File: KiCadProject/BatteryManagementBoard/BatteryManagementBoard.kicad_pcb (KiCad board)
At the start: 6 copper layers, 45 x 45 mm, 86 parts, among them J201 USB-C-2.0, J202 XT30, J203 Conn_02x05, J204 XT60, J205 Conn_02x05, J206 Conn_01x02_Male, J207 Conn_01x05_Male, J208 JST_B5B_XH, Q301 NFET_Gatenames, Q302 NFET_Gatenames, Q303 NFET_Gatenames, Q304 NFET_Gatenames, Q305 PMOS_Gatenames, U301 BQ25713, U401 BD433M5FP, U501 PTN5150

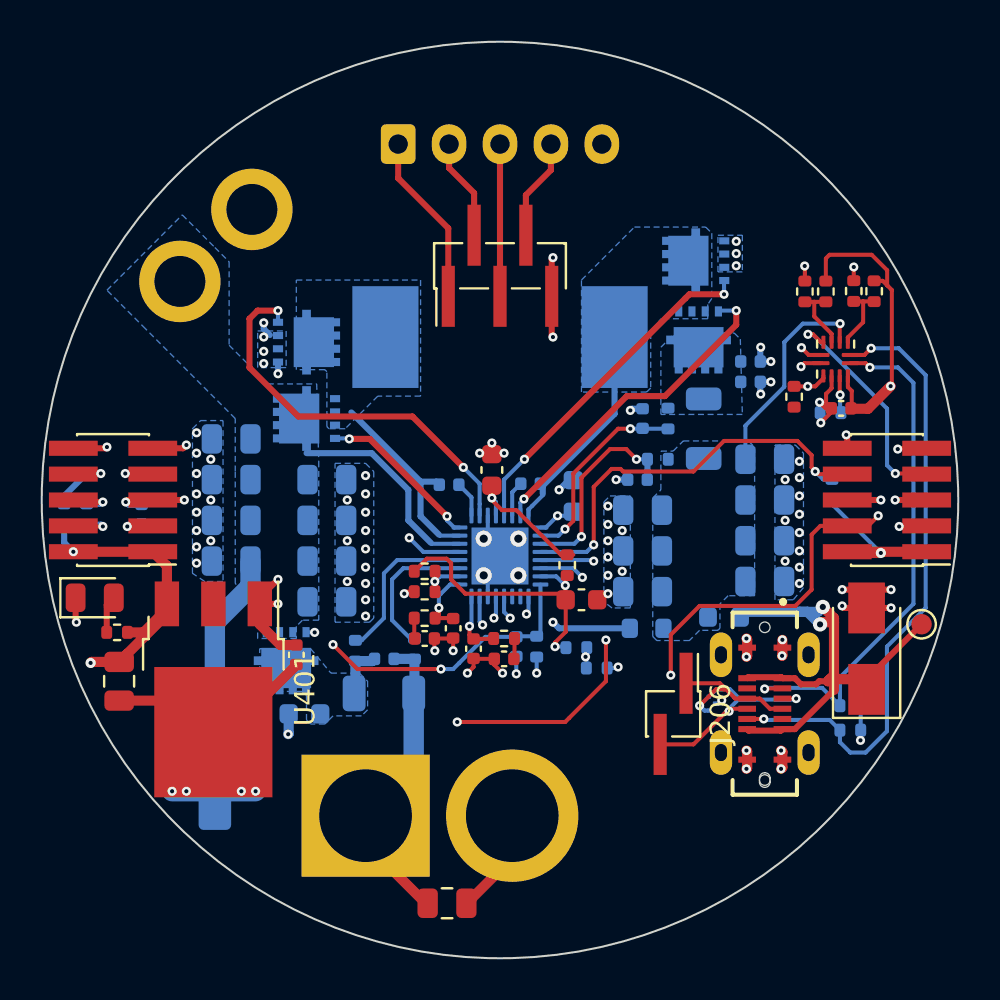
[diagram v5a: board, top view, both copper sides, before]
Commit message: Finished v0.1 of BatMan PCB, started layout of ESP PCB
Signed-off-by: Eldalote.Electronics <Eldalote.Electronics@gmail.com>
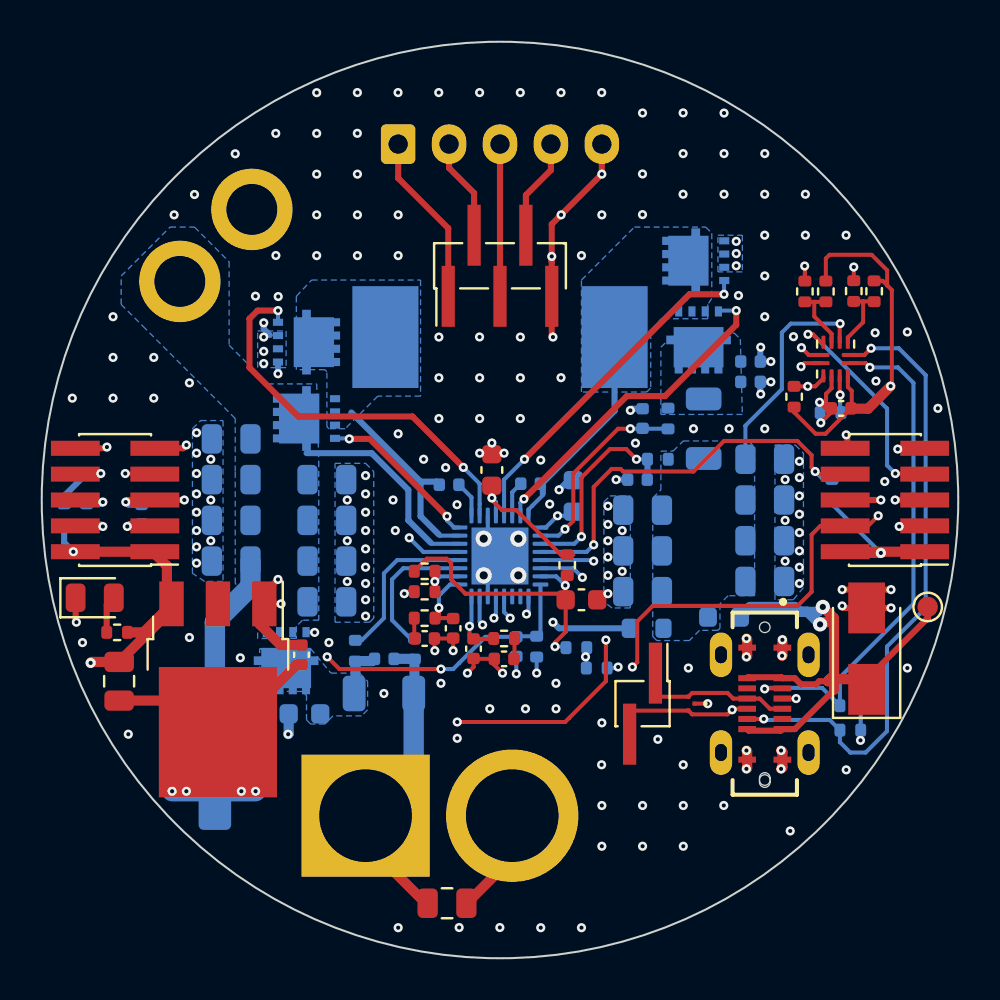
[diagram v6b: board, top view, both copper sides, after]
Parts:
- D202: moved to F.Cu
- moved J206 1.58 mm to (157.0, 110.0)
- moved D202 1.00 mm to (159.4, 110.0)
- moved TP201 0.90 mm to (171.0, 105.2)
- moved C402 0.25 mm to (140.2, 107.6)
- moved U401 0.22 mm to (136.2, 109.3)
- moved J203 0.10 mm to (168.9, 100.0)
- moved J205 0.10 mm to (131.1, 100.0)
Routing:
- net GND: track 76.9 -> 83.7 mm, vias 106 -> 221
- net +3.3V: track 110.0 -> 113.4 mm
- net /P2-Connectors/VBUS_connector: track 26.9 -> 28.0 mm
- net BQ_IADPT: track 31.7 -> 31.2 mm
- net /P2-Connectors/USB-N: track 7.40 -> 7.76 mm, vias 1 -> 0
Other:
- board text added: "Battery"
- board text added: "LED power"

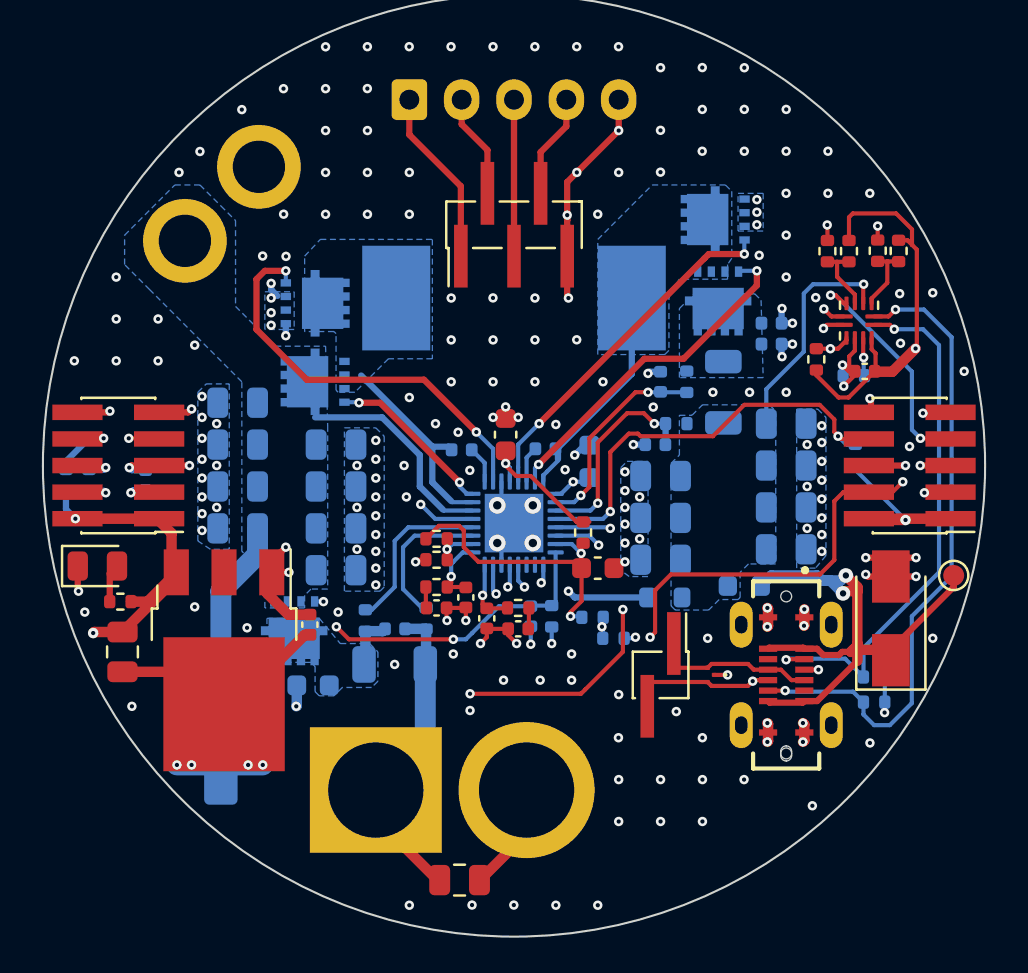
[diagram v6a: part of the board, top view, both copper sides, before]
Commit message: All PCB's should be done. Do a final check before ordering.
Signed-off-by: Eldalote.Electronics <Eldalote.Electronics@gmail.com>
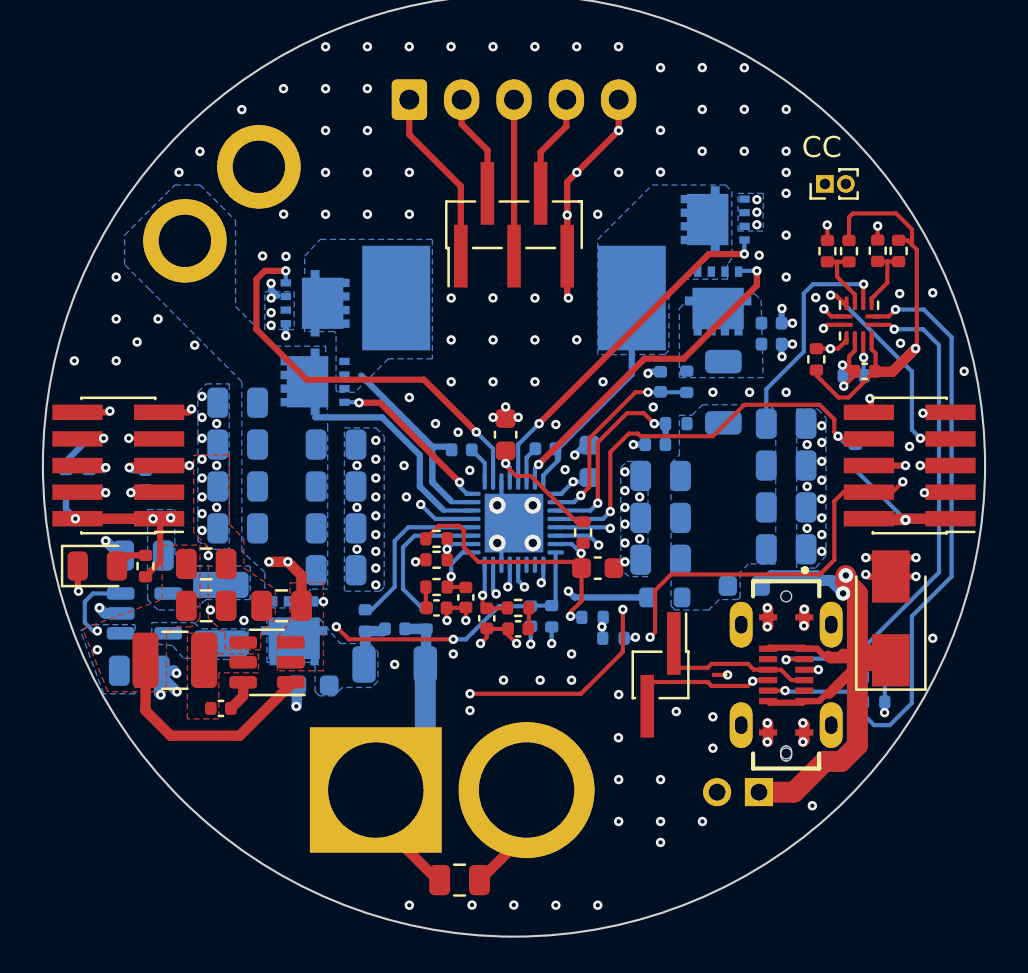
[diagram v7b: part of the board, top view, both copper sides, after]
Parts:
- removed C401: 22u, Capacitor_SMD:CP_Elec_5x5.3
- removed TP201: TestPoint, TestPoint:TestPoint_Pad_D1.0mm
- added C404: 22u, Capacitor_SMD:C_0805_2012Metric, F.Cu at (135.3, 106.7)
- added C405: 22u, Capacitor_SMD:C_0805_2012Metric, F.Cu at (135.3, 104.7)
- added C406: 10u, Capacitor_SMD:C_0805_2012Metric, B.Cu at (132.1, 109.8)
- added C407: 22u, Capacitor_SMD:C_0805_2012Metric, B.Cu at (132.3, 104.3)
- added J209: Optional off board USB power connection, Connector_PinHeader_2.00mm:PinHeader_1x02_P2.00mm_Vertical, B.Cu at (161.7, 115.6)
- added J210: Optional off board USB CC connection, Connector_PinHeader_1.00mm:PinHeader_1x02_P1.00mm_Vertical, F.Cu at (164.8, 86.5)
- added L401: 4u7, Inductor_SMD:L_1210_3225Metric, F.Cu at (133.8, 109.3)
- added L402: 1u, Inductor_SMD:L_1210_3225Metric, B.Cu at (136.0, 107.1)
- added U402: SC189, Package_TO_SOT_SMD:SOT-23-5, B.Cu at (132.3, 107.1)
- C402: value 100n -> 10u; footprint Capacitor_SMD:C_0402_1005Metric -> Capacitor_SMD:C_0805_2012Metric
- C403: value 10u -> 100n; footprint Capacitor_SMD:C_0805_2012Metric -> Capacitor_SMD:C_0402_1005Metric
- U401: value BD433M5FP -> AP63205WU; footprint Package_TO_SOT_SMD:TO-252-3_TabPin4 -> Package_TO_SOT_SMD:TSOT-23-6
- moved C403 5.42 mm to (136.0, 111.6), turned to 0 degrees
- moved R401 2.08 mm to (132.4, 104.8), turned to 90 degrees
- moved U401 2.05 mm to (138.2, 109.4), turned to 180 degrees
- moved C402 1.62 mm to (138.9, 106.7), turned to 180 degrees
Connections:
- C403 pad 1: +3.3V -> /P4 - 3V3 Regulator/APSW
- C403 pad 2: GND -> /P4 - 3V3 Regulator/APBST
- U401 pad 1: VOUT -> +5V
- U401 pad 2: unconnected-(U401-Pad2) -> VOUT
- U401 pad 3: +3.3V -> VOUT
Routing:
- net +5V: track 0.00 -> 14.6 mm, vias 0 -> 2
- net /P2-Connectors/VBUS_connector: track 28.0 -> 40.8 mm
- net VOUT: track 24.1 -> 13.5 mm
- net GND: track 83.7 -> 74.5 mm, vias 221 -> 216
- net CC1: track 25.8 -> 35.0 mm
- net CC2: track 31.0 -> 38.4 mm
- net +3.3V: track 113.4 -> 111.2 mm, vias 4 -> 5
- net /P4 - 3V3 Regulator/APBST: track 0.00 -> 1.49 mm
- added copper zone on B.Cu, net +3.3V
- added copper zone on B.Cu, net +5V
- added copper zone on F.Cu, net +5V
- added copper zone on F.Cu, net /P4 - 3V3 Regulator/APSW
- added copper zone on B.Cu, net /P4 - 3V3 Regulator/scLX
- added copper zone on F.Cu, net GND
- added copper zone on F.Cu, net VOUT
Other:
- board text added: "BM V0.3"
- board text added: "CC"
- board text added: "JM Liewes"
- board text added: "jlcjlcjlcjlc"

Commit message: Made ready to order PCBs. Some problems with ordering due to misunderstanding. Thinking about solutions
Signed-off-by: Eldalote.Electronics <Eldalote.Electronics@gmail.com>
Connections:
- net /P5-TUSB422 (Optional)/PTN_ADR renamed /P5-PTN5150 (Optional)/PTN_ADR
- net /P5-TUSB422 (Optional)/PTN_ENB renamed /P5-PTN5150 (Optional)/PTN_ENB
- net /P5-TUSB422 (Optional)/PTN_PORT renamed /P5-PTN5150 (Optional)/PTN_PORT
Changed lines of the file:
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@@
       (layerselection 0x00010fc_ffffffff)
       (disableapertmacros false)
-      (usegerberextensions false)
+      (usegerberextensions true)
       (usegerberattributes true)
-      (usegerberadvancedattributes true)
-      (creategerberjobfile true)
+      (usegerberadvancedattributes false)
+      (creategerberjobfile false)
       (svguseinch false)
       (svgprecision 6)
@@
       (plotinvisibletext false)
       (sketchpadsonfab false)
-      (subtractmaskfromsilk false)
+      (subtractmaskfromsilk true)
       (outputformat 1)
       (mirror false)
@@
   (net 55 "/P2-Connectors/Cell2")
   (net 56 "/P2-Connectors/Cell1")
-  (net 57 "/P5-TUSB422 (Optional)/PTN_ADR")
-  (net 58 "/P5-TUSB422 (Optional)/PTN_PORT")
-  (net 59 "/P5-TUSB422 (Optional)/PTN_ENB")
+  (net 57 "/P5-PTN5150 (Optional)/PTN_ADR")
+  (net 58 "/P5-PTN5150 (Optional)/PTN_PORT")
+  (net 59 "/P5-PTN5150 (Optional)/PTN_ENB")
   (net 60 "PTN_ID")
   (net 61 "/P4 - 3V3 Regulator/APBST")
@@
     (descr "Texas  X2QFN, 12 Pin (http://www.ti.com/lit/ml/mpqf391c/mpqf391c.pdf), generated with kicad-footprint-generator ipc_noLead_generator.py")
     (tags "Texas X2QFN NoLead")
-    (property "Sheetfile" "P5TUSB422.kicad_sch")
-    (property "Sheetname" "P5-TUSB422 (Optional)")
+    (property "Sheetfile" "P5PTN5150.kicad_sch")
+    (property "Sheetname" "P5-PTN5150 (Optional)")
     (clearance 0.13)
     (attr smd)
@@
       (net 28 "CC2") (pinfunction "CC2") (pintype "passive"))
     (pad "3" smd roundrect (at -0.6 0.825 180) (size 0.2 0.65) (layers "F.Cu" "F.Paste" "F.Mask") (roundrect_rratio 0.25)
-      (net 58 "/P5-TUSB422 (Optional)/PTN_PORT") (pinfunction "PORT") (pintype "passive"))
+      (net 58 "/P5-PTN5150 (Optional)/PTN_PORT") (pinfunction "PORT") (pintype "passive"))
     (pad "4" smd roundrect (at -0.2 0.825 180) (size 0.2 0.65) (layers "F.Cu" "F.Paste" "F.Mask") (roundrect_rratio 0.25)
       (net 1 "VBUS") (pinfunction "VBUS_DET") (pintype "passive"))
     (pad "5" smd roundrect (at 0.2 0.825 180) (size 0.2 0.65) (layers "F.Cu" "F.Paste" "F.Mask") (roundrect_rratio 0.25)
-      (net 57 "/P5-TUSB422 (Optional)/PTN_ADR") (pinfunction "ADR/CON_DET") (pintype "passive"))
+      (net 57 "/P5-PTN5150 (Optional)/PTN_ADR") (pinfunction "ADR/CON_DET") (pintype "passive"))
     (pad "6" smd roundrect (at 0.6 0.825 180) (size 0.2 0.65) (layers "F.Cu" "F.Paste" "F.Mask") (roundrect_rratio 0.25)
       (net 34 "USBC_INT") (pinfunction "INTB") (pintype "passive"))
@@
       (net 2 "GND") (pinfunction "GND") (pintype "passive"))
     (pad "11" smd roundrect (at -0.2 -0.825 180) (size 0.2 0.65) (layers "F.Cu" "F.Paste" "F.Mask") (roundrect_rratio 0.25)
-      (net 59 "/P5-TUSB422 (Optional)/PTN_ENB") (pinfunction "ENB") (pintype "passive"))
+      (net 59 "/P5-PTN5150 (Optional)/PTN_ENB") (pinfunction "ENB") (pintype "passive"))
     (pad "12" smd roundrect (at -0.6 -0.825 180) (size 0.2 0.65) (layers "F.Cu" "F.Paste" "F.Mask") (roundrect_rratio 0.25)
       (net 22 "+3.3V") (pinfunction "VDD") (pintype "passive"))
@@
     (property "Extra Requirement" "25V")
     (property "MfID" "CL05A104KA5NNNC")
-    (property "Sheetfile" "P5TUSB422.kicad_sch")
-    (property "Sheetname" "P5-TUSB422 (Optional)")
+    (property "Sheetfile" "P5PTN5150.kicad_sch")
+    (property "Sheetname" "P5-PTN5150 (Optional)")
     (attr smd)
     (fp_text reference "C501" (at 0 -1.16) (layer "F.Fab")
@@
     (tags "resistor")
     (property "MfID" "CR0402-FX-1002GLF")
-    (property "Sheetfile" "P5TUSB422.kicad_sch")
-    (property "Sheetname" "P5-TUSB422 (Optional)")
+    (property "Sheetfile" "P5PTN5150.kicad_sch")
+    (property "Sheetname" "P5-PTN5150 (Optional)")
     (attr smd)
     (fp_text reference "R506" (at 0 -1.17 90) (layer "F.Fab")
@@
     (descr "Resistor SMD 0402 (1005 Metric), square (rectangular) end terminal, IPC_7351 nominal, (Body size source: IPC-SM-782 page 72, https://www.pcb-3d.com/wordpress/wp-content/uploads/ipc-sm-782a_amendment_1_and_2.pdf), generated with kicad-footprint-generator")
     (tags "resistor")
-    (property "Sheetfile" "P5TUSB422.kicad_sch")
-    (property "Sheetname" "P5-TUSB422 (Optional)")
+    (property "Sheetfile" "P5PTN5150.kicad_sch")
+    (property "Sheetname" "P5-PTN5150 (Optional)")
     (attr smd)
     (fp_text reference "R502" (at 0 -1.17 90) (layer "F.Fab")
@@
       (net 2 "GND") (pintype "passive"))
     (pad "2" smd roundrect (at 0.51 0 270) (size 0.54 0.64) (layers "F.Cu" "F.Paste" "F.Mask") (roundrect_rratio 0.25)
-      (net 57 "/P5-TUSB422 (Optional)/PTN_ADR") (pintype "passive"))
+      (net 57 "/P5-PTN5150 (Optional)/PTN_ADR") (pintype "passive"))
     (model "${KICAD6_3DMODEL_DIR}/Resistor_SMD.3dshapes/R_0402_1005Metric.wrl"
       (offset (xyz 0 0 0))
@@
     (tags "resistor")
     (property "MfID" "CR0402-FX-1002GLF")
-    (property "Sheetfile" "P5TUSB422.kicad_sch")
-    (property "Sheetname" "P5-TUSB422 (Optional)")
+    (property "Sheetfile" "P5PTN5150.kicad_sch")
+    (property "Sheetname" "P5-PTN5150 (Optional)")
     (attr smd)
     (fp_text reference "R503" (at 0 -1.17 90) (layer "F.Fab")
@@
     (fp_line (start -0.525 -0.27) (end 0.525 -0.27) (layer "F.Fab") (width 0.1))
     (pad "1" smd roundrect (at -0.51 0 90) (size 0.54 0.64) (layers "F.Cu" "F.Paste" "F.Mask") (roundrect_rratio 0.25)
-      (net 58 "/P5-TUSB422 (Optional)/PTN_PORT") (pintype "passive"))
+      (net 58 "/P5-PTN5150 (Optional)/PTN_PORT") (pintype "passive"))
     (pad "2" smd roundrect (at 0.51 0 90) (size 0.54 0.64) (layers "F.Cu" "F.Paste" "F.Mask") (roundrect_rratio 0.25)
       (net 22 "+3.3V") (pintype "passive"))
@@
     (descr "Resistor SMD 0402 (1005 Metric), square (rectangular) end terminal, IPC_7351 nominal, (Body size source: IPC-SM-782 page 72, https://www.pcb-3d.com/wordpress/wp-content/uploads/ipc-sm-782a_amendment_1_and_2.pdf), generated with kicad-footprint-generator")
     (tags "resistor")
-    (property "Sheetfile" "P5TUSB422.kicad_sch")
-    (property "Sheetname" "P5-TUSB422 (Optional)")
+    (property "Sheetfile" "P5PTN5150.kicad_sch")
+    (property "Sheetname" "P5-PTN5150 (Optional)")
     (attr smd)
     (fp_text reference "R504" (at 0 -1.17 90) (layer "F.Fab")
@@
       (net 2 "GND") (pintype "passive"))
     (pad "2" smd roundrect (at 0.51 0 270) (size 0.54 0.64) (layers "F.Cu" "F.Paste" "F.Mask") (roundrect_rratio 0.25)
-      (net 58 "/P5-TUSB422 (Optional)/PTN_PORT") (pintype "passive"))
+      (net 58 "/P5-PTN5150 (Optional)/PTN_PORT") (pintype "passive"))
     (model "${KICAD6_3DMODEL_DIR}/Resistor_SMD.3dshapes/R_0402_1005Metric.wrl"
       (offset (xyz 0 0 0))
@@
     (tags "resistor")
     (property "MfID" "CR0402-FX-1002GLF")
-    (property "Sheetfile" "P5TUSB422.kicad_sch")
-    (property "Sheetname" "P5-TUSB422 (Optional)")
+    (property "Sheetfile" "P5PTN5150.kicad_sch")
+    (property "Sheetname" "P5-PTN5150 (Optional)")
     (attr smd)
     (fp_text reference "R501" (at 0 -1.17 90) (layer "F.Fab")
@@
     (fp_line (start -0.525 -0.27) (end 0.525 -0.27) (layer "F.Fab") (width 0.1))
     (pad "1" smd roundrect (at -0.51 0 90) (size 0.54 0.64) (layers "F.Cu" "F.Paste" "F.Mask") (roundrect_rratio 0.25)
-      (net 57 "/P5-TUSB422 (Optional)/PTN_ADR") (pintype "passive"))
+      (net 57 "/P5-PTN5150 (Optional)/PTN_ADR") (pintype "passive"))
     (pad "2" smd roundrect (at 0.51 0 90) (size 0.54 0.64) (layers "F.Cu" "F.Paste" "F.Mask") (roundrect_rratio 0.25)
       (net 22 "+3.3V") (pintype "passive"))
@@
     (tags "resistor")
     (property "MfID" "CR0402-FX-1002GLF")
-    (property "Sheetfile" "P5TUSB422.kicad_sch")
-    (property "Sheetname" "P5-TUSB422 (Optional)")
+    (property "Sheetfile" "P5PTN5150.kicad_sch")
+    (property "Sheetname" "P5-PTN5150 (Optional)")
     (attr smd)
     (fp_text reference "R505" (at 0 1.17) (layer "B.Fab")
@@
       (net 2 "GND") (pintype "passive"))
     (pad "2" smd roundrect (at 0.51 0) (size 0.54 0.64) (layers "B.Cu" "B.Paste" "B.Mask") (roundrect_rratio 0.25)
-      (net 59 "/P5-TUSB422 (Optional)/PTN_ENB") (pintype "passive"))
+      (net 59 "/P5-PTN5150 (Optional)/PTN_ENB") (pintype "passive"))
     (model "${KICAD6_3DMODEL_DIR}/Resistor_SMD.3dshapes/R_0402_1005Metric.wrl"
       (offset (xyz 0 0 0))
